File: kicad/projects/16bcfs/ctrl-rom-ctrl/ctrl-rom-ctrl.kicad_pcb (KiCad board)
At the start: 4 copper layers, 0 parts

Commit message: Video 0099 (#147)
Control ROM Control Module PCB Design & Free-Running the Emulator

* Closes #140
* Closes #89
* Closes #141
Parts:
- added C1: 0u1, Capacitor_SMD:C_1206_3216Metric_Pad1.33x1.80mm_HandSolder, B.Cu at (47.0, 48.1)
- added C11: 0u1, Capacitor_SMD:C_1206_3216Metric_Pad1.33x1.80mm_HandSolder, F.Cu at (73.2, 41.7)
- added C12: 0u1, Capacitor_SMD:C_1206_3216Metric_Pad1.33x1.80mm_HandSolder, B.Cu at (94.0, 41.5)
- added C13: 0u1, Capacitor_SMD:C_1206_3216Metric_Pad1.33x1.80mm_HandSolder, F.Cu at (91.2, 41.6)
- added C14: 0u1, Capacitor_SMD:C_1206_3216Metric_Pad1.33x1.80mm_HandSolder, B.Cu at (111.9, 41.6)
- added C15: 0u1, Capacitor_SMD:C_1206_3216Metric_Pad1.33x1.80mm_HandSolder, F.Cu at (73.2, 32.8)
- added C16: 0u1, Capacitor_SMD:C_1206_3216Metric_Pad1.33x1.80mm_HandSolder, B.Cu at (94.0, 32.8)
- added C17: 0u1, Capacitor_SMD:C_1206_3216Metric_Pad1.33x1.80mm_HandSolder, F.Cu at (91.2, 32.8)
- added C18: 0u1, Capacitor_SMD:C_1206_3216Metric_Pad1.33x1.80mm_HandSolder, B.Cu at (111.9, 32.8)
- added C19: 0u1, Capacitor_SMD:C_1206_3216Metric_Pad1.33x1.80mm_HandSolder, B.Cu at (56.4, 48.1)
- added C2: 0u1, Capacitor_SMD:C_1206_3216Metric_Pad1.33x1.80mm_HandSolder, F.Cu at (55.7, 33.3)
- added C20: 0u1, Capacitor_SMD:C_1206_3216Metric_Pad1.33x1.80mm_HandSolder, B.Cu at (34.3, 35.9)
- added C21: 0u1, Capacitor_SMD:C_1206_3216Metric_Pad1.33x1.80mm_HandSolder, F.Cu at (32.1, 62.6)
- added C22: 0u1, Capacitor_SMD:C_1206_3216Metric_Pad1.33x1.80mm_HandSolder, F.Cu at (46.1, 62.6)
- added C23: 0u1, Capacitor_SMD:C_1206_3216Metric_Pad1.33x1.80mm_HandSolder, F.Cu at (43.5, 48.5)
- added C24: 47u, Capacitor_SMD:C_1206_3216Metric_Pad1.33x1.80mm_HandSolder, F.Cu at (108.6, 58.4)
- added C25: 47u, Capacitor_SMD:C_1206_3216Metric_Pad1.33x1.80mm_HandSolder, B.Cu at (31.1, 58.4)
- added C3: 0u1, Capacitor_SMD:C_1206_3216Metric_Pad1.33x1.80mm_HandSolder, B.Cu at (37.4, 48.0)
- added C4: 0u1, Capacitor_SMD:C_1206_3216Metric_Pad1.33x1.80mm_HandSolder, F.Cu at (28.9, 48.6)
- added C5: 0u1, Capacitor_SMD:C_1206_3216Metric_Pad1.33x1.80mm_HandSolder, B.Cu at (74.4, 59.5)
- added C6: 0u1, Capacitor_SMD:C_1206_3216Metric_Pad1.33x1.80mm_HandSolder, F.Cu at (56.2, 48.9)
- added C7: 0u1, Capacitor_SMD:C_1206_3216Metric_Pad1.33x1.80mm_HandSolder, F.Cu at (64.3, 33.4)
- added C8: 0u1, Capacitor_SMD:C_1206_3216Metric_Pad1.33x1.80mm_HandSolder, B.Cu at (93.5, 59.6)
- added C9: 0u1, Capacitor_SMD:C_1206_3216Metric_Pad1.33x1.80mm_HandSolder, B.Cu at (58.4, 32.1)
- added D1: Red, LED_SMD:LED_1206_3216Metric_Pad1.42x1.75mm_HandSolder, F.Cu at (73.0, 65.7)
- added D10: Red, LED_SMD:LED_1206_3216Metric_Pad1.42x1.75mm_HandSolder, F.Cu at (95.9, 65.7)
- added D11: Red, LED_SMD:LED_1206_3216Metric_Pad1.42x1.75mm_HandSolder, F.Cu at (98.4, 65.7)
- added D12: Red, LED_SMD:LED_1206_3216Metric_Pad1.42x1.75mm_HandSolder, F.Cu at (101.0, 65.7)
- added D13: Red, LED_SMD:LED_1206_3216Metric_Pad1.42x1.75mm_HandSolder, F.Cu at (103.5, 65.7)
- added D14: Red, LED_SMD:LED_1206_3216Metric_Pad1.42x1.75mm_HandSolder, F.Cu at (106.0, 65.7)
- added D15: Red, LED_SMD:LED_1206_3216Metric_Pad1.42x1.75mm_HandSolder, F.Cu at (108.6, 65.7)
- added D2: Red, LED_SMD:LED_1206_3216Metric_Pad1.42x1.75mm_HandSolder, F.Cu at (75.6, 65.7)
- added D24: Red, LED_SMD:LED_1206_3216Metric_Pad1.42x1.75mm_HandSolder, F.Cu at (111.1, 65.7)
- added D3: Red, LED_SMD:LED_1206_3216Metric_Pad1.42x1.75mm_HandSolder, F.Cu at (78.1, 65.7)
- added D4: Red, LED_SMD:LED_1206_3216Metric_Pad1.42x1.75mm_HandSolder, F.Cu at (80.6, 65.7)
- added D5: Red, LED_SMD:LED_1206_3216Metric_Pad1.42x1.75mm_HandSolder, F.Cu at (83.2, 65.7)
- added D6: Red, LED_SMD:LED_1206_3216Metric_Pad1.42x1.75mm_HandSolder, F.Cu at (85.7, 65.7)
- added D7: Red, LED_SMD:LED_1206_3216Metric_Pad1.42x1.75mm_HandSolder, F.Cu at (88.3, 65.7)
- added D8: Red, LED_SMD:LED_1206_3216Metric_Pad1.42x1.75mm_HandSolder, F.Cu at (90.8, 65.7)
- added D9: Red, LED_SMD:LED_1206_3216Metric_Pad1.42x1.75mm_HandSolder, F.Cu at (93.3, 65.7)
- added J1: Instruction, Connector_PinHeader_2.54mm:PinHeader_1x16_P2.54mm_Vertical, B.Cu at (69.8, 27.9)
- added J2: Control ROM Address, Connector_PinHeader_2.54mm:PinHeader_1x16_P2.54mm_Vertical, B.Cu at (73.7, 48.3)
- added J3: Raw Address for Pgm ROM, Connector_PinHeader_2.54mm:PinHeader_1x16_P2.54mm_Vertical, B.Cu at (73.7, 27.9)
- added J4: Signal Header, Connector_PinHeader_2.54mm:PinHeader_1x16_P2.54mm_Vertical, B.Cu at (27.9, 27.9)
- added J5: Power, Connector_PinHeader_2.54mm:PinHeader_1x02_P2.54mm_Vertical, B.Cu at (27.9, 57.1)
- added J6: Power, Connector_PinHeader_2.54mm:PinHeader_1x02_P2.54mm_Vertical, B.Cu at (111.8, 57.1)
- added R1: 1K, Resistor_SMD:R_1206_3216Metric_Pad1.30x1.75mm_HandSolder, B.Cu at (73.0, 65.8)
- added R10: 1K, Resistor_SMD:R_1206_3216Metric_Pad1.30x1.75mm_HandSolder, B.Cu at (95.9, 65.8)
- added R11: 1K, Resistor_SMD:R_1206_3216Metric_Pad1.30x1.75mm_HandSolder, B.Cu at (98.4, 65.8)
- added R12: 1K, Resistor_SMD:R_1206_3216Metric_Pad1.30x1.75mm_HandSolder, B.Cu at (101.0, 65.8)
- added R13: 1K, Resistor_SMD:R_1206_3216Metric_Pad1.30x1.75mm_HandSolder, B.Cu at (103.5, 65.8)
- added R14: 1K, Resistor_SMD:R_1206_3216Metric_Pad1.30x1.75mm_HandSolder, B.Cu at (106.0, 65.8)
- added R15: 1K, Resistor_SMD:R_1206_3216Metric_Pad1.30x1.75mm_HandSolder, B.Cu at (108.6, 65.8)
- added R16: 0R, Resistor_SMD:R_1206_3216Metric_Pad1.30x1.75mm_HandSolder, F.Cu at (42.6, 56.9)
- added R17: 0R, Resistor_SMD:R_1206_3216Metric_Pad1.30x1.75mm_HandSolder, F.Cu at (45.1, 56.9)
- added R18: 0R, Resistor_SMD:R_1206_3216Metric_Pad1.30x1.75mm_HandSolder, B.Cu at (64.7, 48.6)
- added R19: 0R, Resistor_SMD:R_1206_3216Metric_Pad1.30x1.75mm_HandSolder, B.Cu at (64.7, 45.9)
- added R2: 1K, Resistor_SMD:R_1206_3216Metric_Pad1.30x1.75mm_HandSolder, B.Cu at (75.6, 65.8)
- added R20: 0R, Resistor_SMD:R_1206_3216Metric_Pad1.30x1.75mm_HandSolder, F.Cu at (47.6, 56.9)
- added R21: 0R, Resistor_SMD:R_1206_3216Metric_Pad1.30x1.75mm_HandSolder, B.Cu at (64.7, 51.3)
- added R22: 0R, Resistor_SMD:R_1206_3216Metric_Pad1.30x1.75mm_HandSolder, F.Cu at (65.2, 63.9)
- added R23: 0R, Resistor_SMD:R_1206_3216Metric_Pad1.30x1.75mm_HandSolder, F.Cu at (65.2, 61.4)
- added R24: 1K, Resistor_SMD:R_1206_3216Metric_Pad1.30x1.75mm_HandSolder, B.Cu at (111.1, 65.8)
- added R25: 0R, Resistor_SMD:R_1206_3216Metric_Pad1.30x1.75mm_HandSolder, B.Cu at (48.5, 38.1)
- added R26: 0R, Resistor_SMD:R_1206_3216Metric_Pad1.30x1.75mm_HandSolder, B.Cu at (43.2, 33.3)
- added R27: 0R, Resistor_SMD:R_1206_3216Metric_Pad1.30x1.75mm_HandSolder, F.Cu at (65.2, 66.4)
- added R28: 0R, Resistor_SMD:R_1206_3216Metric_Pad1.30x1.75mm_HandSolder, F.Cu at (59.9, 63.9)
- added R29: 0R, Resistor_SMD:R_1206_3216Metric_Pad1.30x1.75mm_HandSolder, F.Cu at (59.9, 61.4)
- added R3: 1K, Resistor_SMD:R_1206_3216Metric_Pad1.30x1.75mm_HandSolder, B.Cu at (78.1, 65.8)
- added R30: 0R, Resistor_SMD:R_1206_3216Metric_Pad1.30x1.75mm_HandSolder, F.Cu at (59.9, 66.4)
- added R31: 0R, Resistor_SMD:R_1206_3216Metric_Pad1.30x1.75mm_HandSolder, F.Cu at (33.7, 56.9)
- added R32: 0R, Resistor_SMD:R_1206_3216Metric_Pad1.30x1.75mm_HandSolder, F.Cu at (39.1, 56.9)
- added R33: 0R, Resistor_SMD:R_1206_3216Metric_Pad1.30x1.75mm_HandSolder, F.Cu at (36.4, 56.9)
- added R34: 0R, Resistor_SMD:R_1206_3216Metric_Pad1.30x1.75mm_HandSolder, B.Cu at (38.4, 63.5)
- added R35: 0R, Resistor_SMD:R_1206_3216Metric_Pad1.30x1.75mm_HandSolder, B.Cu at (41.1, 63.5)
- added R36: 0R, Resistor_SMD:R_1206_3216Metric_Pad1.30x1.75mm_HandSolder, B.Cu at (35.7, 63.5)
- added R4: 1K, Resistor_SMD:R_1206_3216Metric_Pad1.30x1.75mm_HandSolder, B.Cu at (80.6, 65.8)
- added R5: 1K, Resistor_SMD:R_1206_3216Metric_Pad1.30x1.75mm_HandSolder, B.Cu at (83.2, 65.8)
- added R6: 1K, Resistor_SMD:R_1206_3216Metric_Pad1.30x1.75mm_HandSolder, B.Cu at (85.7, 65.8)
- added R7: 1K, Resistor_SMD:R_1206_3216Metric_Pad1.30x1.75mm_HandSolder, B.Cu at (88.3, 65.8)
- added R8: 1K, Resistor_SMD:R_1206_3216Metric_Pad1.30x1.75mm_HandSolder, B.Cu at (90.8, 65.8)
- added R9: 1K, Resistor_SMD:R_1206_3216Metric_Pad1.30x1.75mm_HandSolder, B.Cu at (93.3, 65.8)
- added U1: 74HC08, Package_SO:SOIC-14_3.9x8.7mm_P1.27mm, B.Cu at (47.8, 54.4)
- added U11: 74HC157, Package_SO:SOIC-16_3.9x9.9mm_P1.27mm, F.Cu at (79.8, 42.5)
- added U12: 74HC157, Package_SO:SOIC-16_3.9x9.9mm_P1.27mm, B.Cu at (87.4, 42.5)
- added U13: 74HC157, Package_SO:SOIC-16_3.9x9.9mm_P1.27mm, F.Cu at (97.8, 42.5)
- added U14: 74HC157, Package_SO:SOIC-16_3.9x9.9mm_P1.27mm, B.Cu at (105.4, 42.5)
- added U15: 74HC193, Package_SO:SOIC-16_3.9x9.9mm_P1.27mm, F.Cu at (79.8, 33.7)
- added U16: 74HC193, Package_SO:SOIC-16_3.9x9.9mm_P1.27mm, B.Cu at (87.4, 33.7)
- added U17: 74HC193, Package_SO:SOIC-16_3.9x9.9mm_P1.27mm, F.Cu at (97.8, 33.7)
- added U18: 74HC193, Package_SO:SOIC-16_3.9x9.9mm_P1.27mm, B.Cu at (105.4, 33.7)
- added U19: 74HC04, Package_SO:SOIC-14_3.9x8.7mm_P1.27mm, B.Cu at (57.2, 54.4)
- added U2: 74HC74, Package_SO:SOIC-14_3.9x8.7mm_P1.27mm, F.Cu at (54.9, 39.3)
- added U21: 74HC08, Package_SO:SOIC-14_3.9x8.7mm_P1.27mm, F.Cu at (38.1, 63.5)
- added U22: 74HC08, Package_SO:SOIC-14_3.9x8.7mm_P1.27mm, F.Cu at (52.1, 63.5)
- added U23: 74HC32, Package_SO:SOIC-14_3.9x8.7mm_P1.27mm, F.Cu at (49.5, 49.5)
- added U3: 74HC03, Package_SO:SOIC-14_3.9x8.7mm_P1.27mm, B.Cu at (38.3, 54.4)
- added U4: 74HC193, Package_SO:SOIC-16_3.9x9.9mm_P1.27mm, F.Cu at (35.6, 49.5)
- added U5: 74HC541, Package_SO:SOIC-20W_7.5x12.8mm_P1.27mm, B.Cu at (82.5, 56.5)
- added U6: 74HC00, Package_SO:SOIC-14_3.9x8.7mm_P1.27mm, F.Cu at (62.2, 49.7)
- added U7: 74HC00, Package_SO:SOIC-14_3.9x8.7mm_P1.27mm, F.Cu at (63.4, 39.4)
- added U8: 74HC541, Package_SO:SOIC-20W_7.5x12.8mm_P1.27mm, B.Cu at (101.6, 56.5)
- added U9: 74HC165, Package_SO:SOIC-16_3.9x9.9mm_P1.27mm, B.Cu at (59.3, 38.7)
- added X1: XO32, eryjus:Oscillator_DIP-8-14, F.Cu at (31.8, 41.9)
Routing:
- net GNDREF: track 0.00 -> 613.1 mm, vias 0 -> 105
- net VCC: track 0.00 -> 303.4 mm, vias 0 -> 39
- net ~{QR}: track 0.00 -> 184.6 mm, vias 0 -> 2
- net ~{DONE}: track 0.00 -> 123.5 mm, vias 0 -> 8
- net CPY_CLK: track 0.00 -> 110.1 mm, vias 0 -> 1
- net SRAM ~{CE}: track 0.00 -> 100.7 mm, vias 0 -> 2
- net ~{Raw_Cpy_Clk}: track 0.00 -> 89.5 mm, vias 0 -> 4
- net ~{RESET}: track 0.00 -> 72.2 mm, vias 0 -> 2
- net QS: track 0.00 -> 71.9 mm, vias 0 -> 4
- net Addr Counter ~{CO}: track 0.00 -> 71.4 mm, vias 0 -> 3
- net QC: track 0.00 -> 64.5 mm, vias 0 -> 8
- net RAW_CPY_CLK: track 0.00 -> 61.7 mm, vias 0 -> 2
- net Net-(U19-Pad13): track 0.00 -> 60.3 mm, vias 0 -> 3
- net INSTR_AC: track 0.00 -> 56.1 mm, vias 0 -> 3
- net INSTR_AE: track 0.00 -> 54.2 mm, vias 0 -> 1
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- added copper zone on B.Cu, net GNDREF
- added copper zone on F.Cu, net GNDREF
- added copper zone on In1.Cu, net GNDREF
- added copper zone on In2.Cu, net VCC
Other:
- board outline added: 88.9 x 43.2 mm
- board text added: "0R"
- board text added: "0u1"
- board text added: "16-Bit Computer From Scratch"
- board text added: "47u"
- board text added: "74HC00"
- board text added: "74HC03"
- board text added: "74HC04"
- board text added: "74HC08"
- board text added: "74HC157"
- board text added: "74HC165"
- board text added: "74HC193"
- board text added: "74HC32"
- board text added: "74HC541"
- board text added: "74HC74"
- board text added: "A"
- board text added: "AND3C"
- board text added: "AND3D"
- board text added: "B"
- board text added: "Control ROM Control Module"
- board text added: "Ctrl ROM Address"
- board text added: "ERYJUS"
- board text added: "GND"
- board text added: "Instruction"
- board text added: "Local Xtal"
- board text added: "NAND2C"
- board text added: "Raw Addr for Pgm ROM"
- board text added: "Raw Sys Clk"
- board text added: "Signals"
- board text added: "VCC"
- board text added: "VCC GND"
- board text added: "Y"
- board text added: "oNANDB"
- board text added: "oNANDC"
- board text added: "oNANDD"
- board text added: "v1.0"

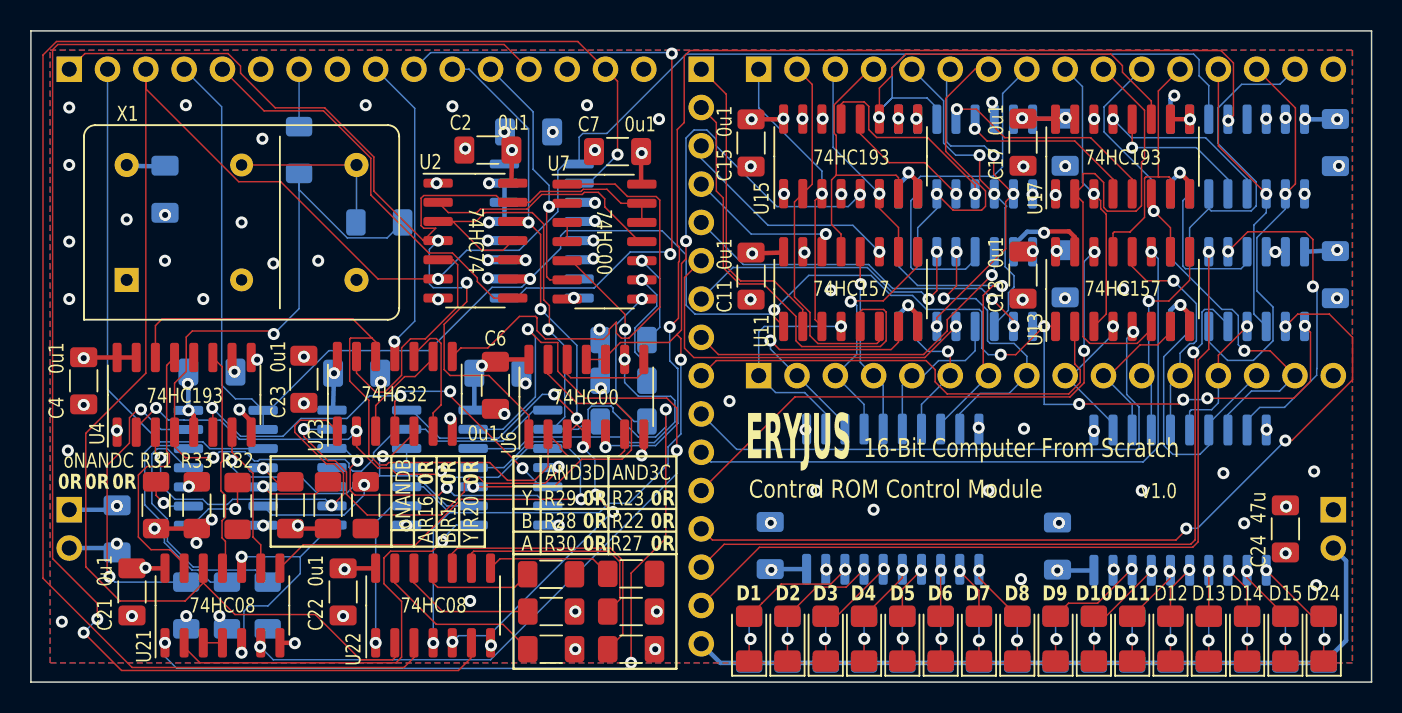
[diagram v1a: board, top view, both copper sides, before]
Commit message: Complete the existing bodge on the PCB
An existing bodge was updated in the schematic and this was extended to
the PCB design of the Control ROM Control Module.

Additionally, the footprints were updated.

I also took the opportunity to update a trace which bounced around a
bit.
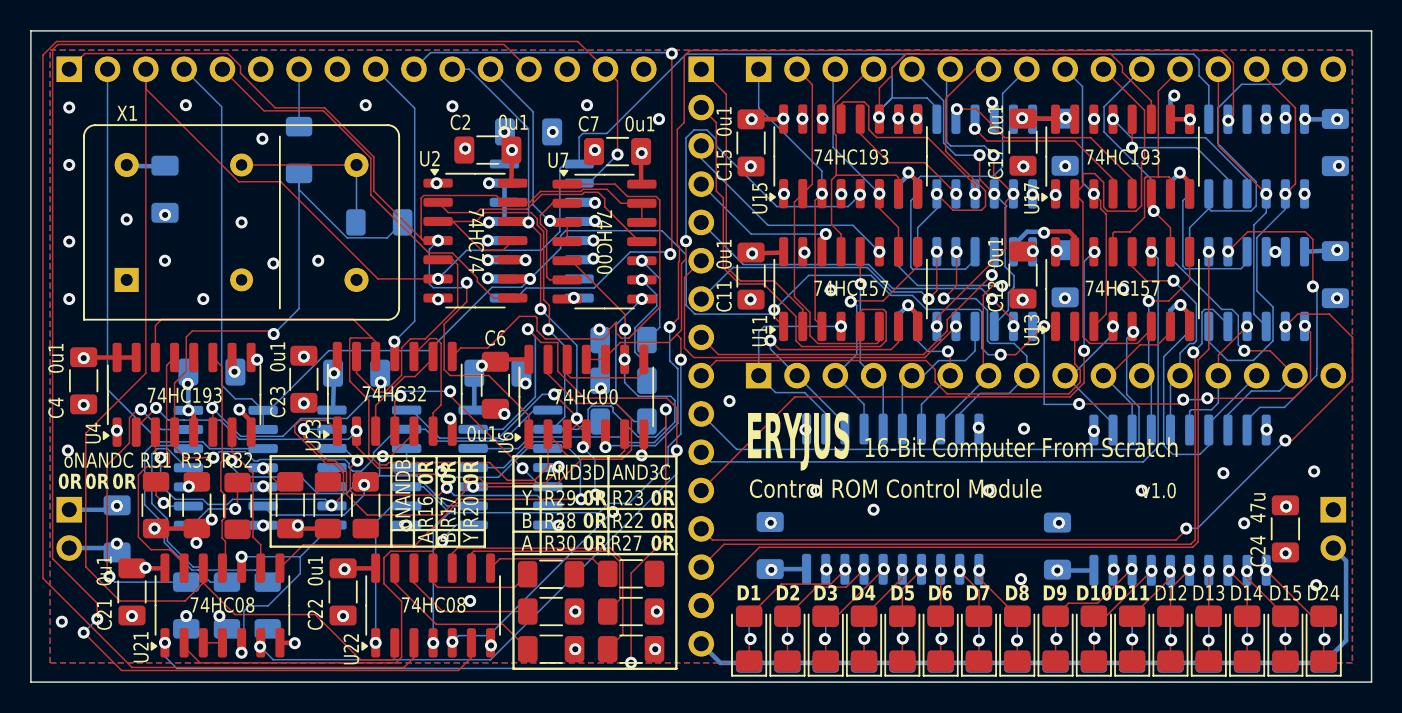
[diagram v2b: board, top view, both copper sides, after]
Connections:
- J4 pad 12: ~{QL} -> QL
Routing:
- net QL: track 1.27 -> 15.4 mm, vias 0 -> 1
- net ~{QL}: track 18.2 -> 7.80 mm, vias 1 -> 0
- net ~{RESET}: track 72.2 -> 71.1 mm
- net ~{QR}: track 184.6 -> 185.4 mm

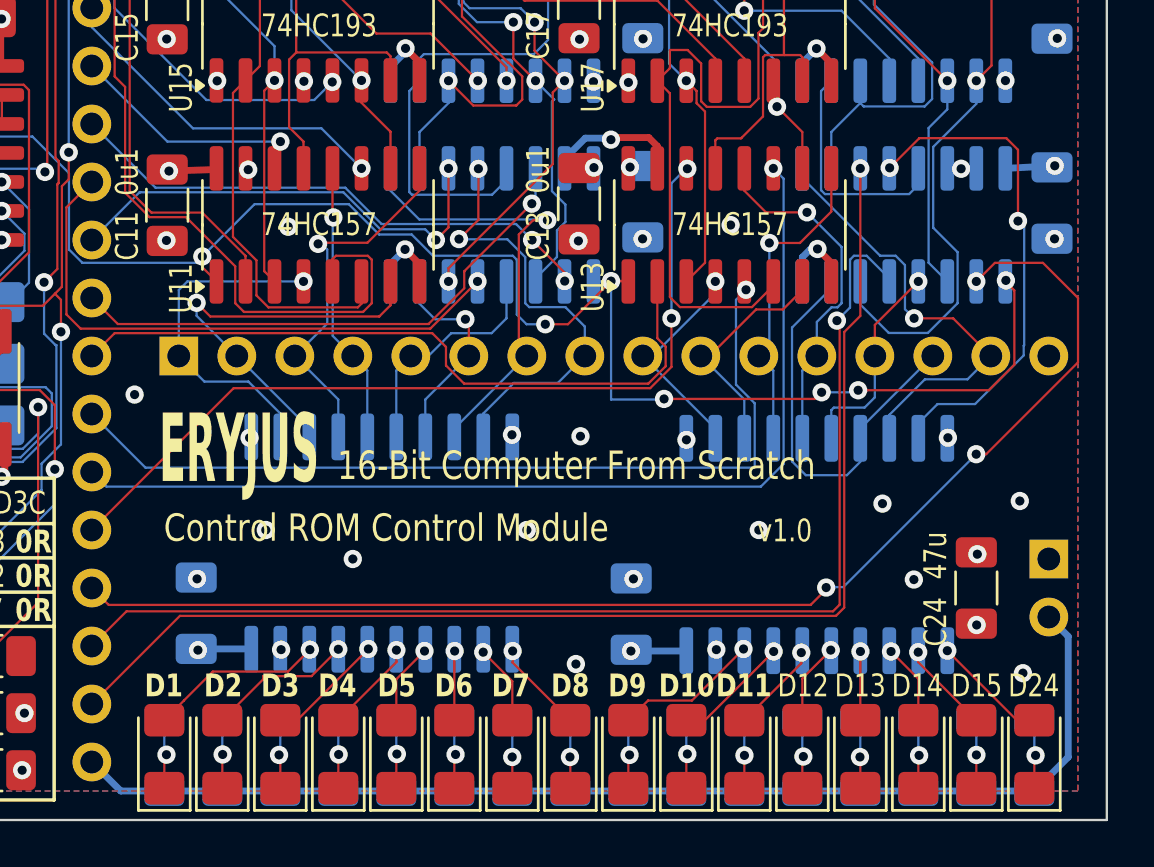
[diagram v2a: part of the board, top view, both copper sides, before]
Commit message: Remove the LEDs from the Control ROM Control Module
The LEDs are not populated on the first iteration PCB.  Remove them from
the schematic and from the PCB design.
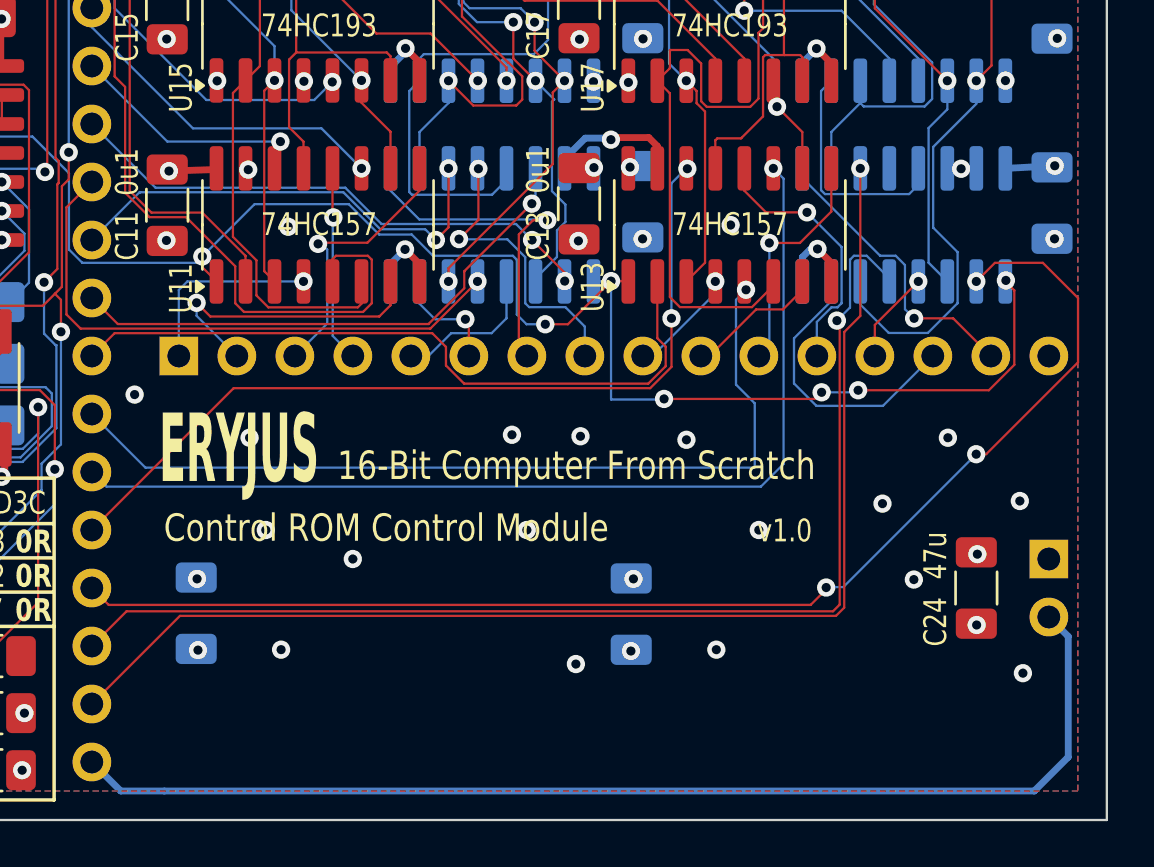
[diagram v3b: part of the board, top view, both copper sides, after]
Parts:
- removed D1, D10, D11, D12, D13, D14, D15, D2, D24, D3, D4, D5, D6, D7, D8, D9: Red, LED_SMD:LED_1206_3216Metric_Pad1.42x1.75mm_HandSolder
- removed R1, R10, R11, R12, R13, R14, R15, R2, R24, R3, R4, R5, R6, R7, R8, R9: 1K, Resistor_SMD:R_1206_3216Metric_Pad1.30x1.75mm_HandSolder
- removed U5, U8: 74HC541, Package_SO:SOIC-20W_7.5x12.8mm_P1.27mm
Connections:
- U14 pad 12: ROM_AF -> unconnected-(U14-Zd-Pad12)
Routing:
- net ROM_AF: track 21.3 -> 0.00 mm, vias 2 -> 0
- net Net-(D1-A): track 7.66 -> 0.00 mm, vias 1 -> 0
- net ROM_AE: track 19.2 -> 12.6 mm
- net ROM_A0: track 15.0 -> 8.51 mm
- net ROM_A7: track 19.5 -> 13.0 mm
- net Net-(D2-A): track 6.45 -> 0.00 mm, vias 1 -> 0
- net Net-(D9-A): track 6.34 -> 0.00 mm, vias 1 -> 0
- net ROM_AC: track 9.24 -> 4.05 mm
- net VCC: track 303.4 -> 298.6 mm
- net ROM_AD: track 17.3 -> 12.5 mm
- net ROM_A6: track 19.4 -> 14.9 mm
- net ROM_A8: track 8.89 -> 4.40 mm
- net ROM_A1: track 17.5 -> 13.0 mm
- net Net-(D3-A): track 4.41 -> 0.00 mm, vias 1 -> 0
- net ROM_A9: track 9.65 -> 5.26 mm
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
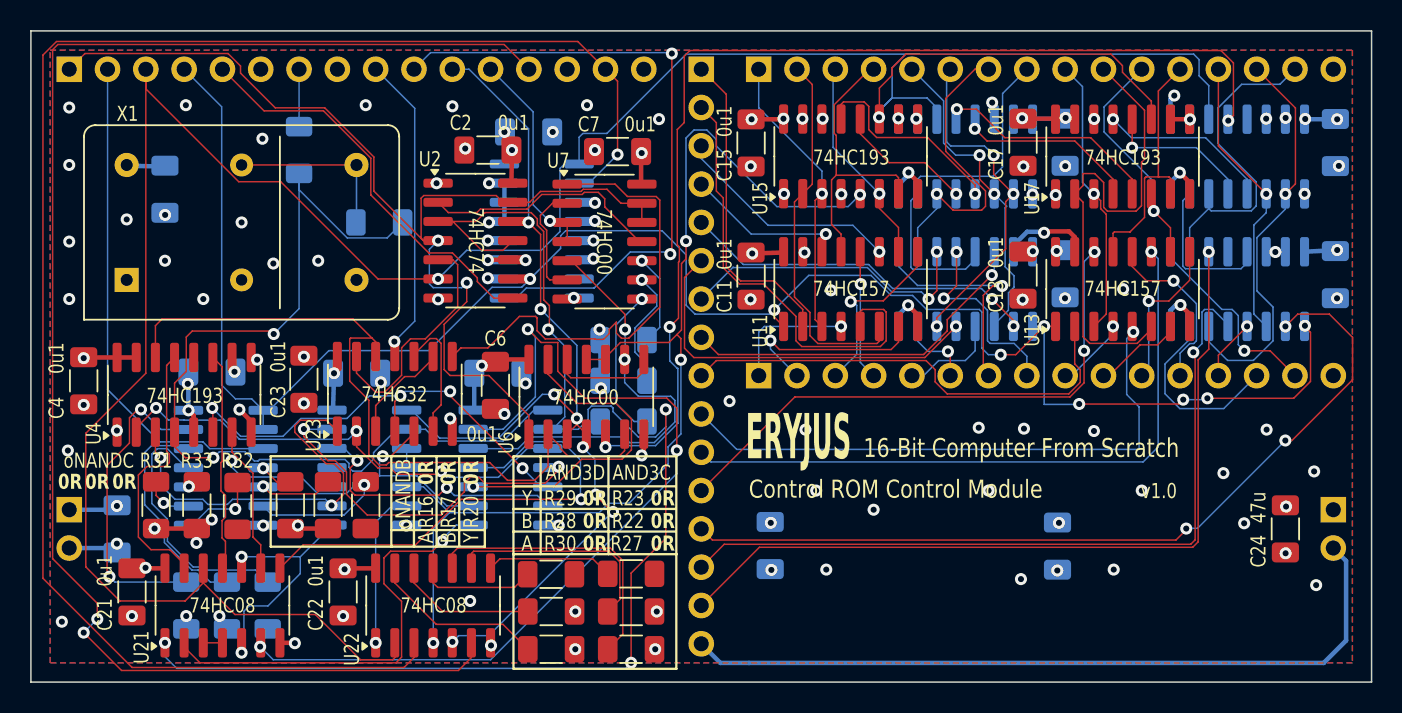
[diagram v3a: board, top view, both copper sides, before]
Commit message: Resolve the Control ROM Control pin alignment
This resulted in a major change to the PCB layout.
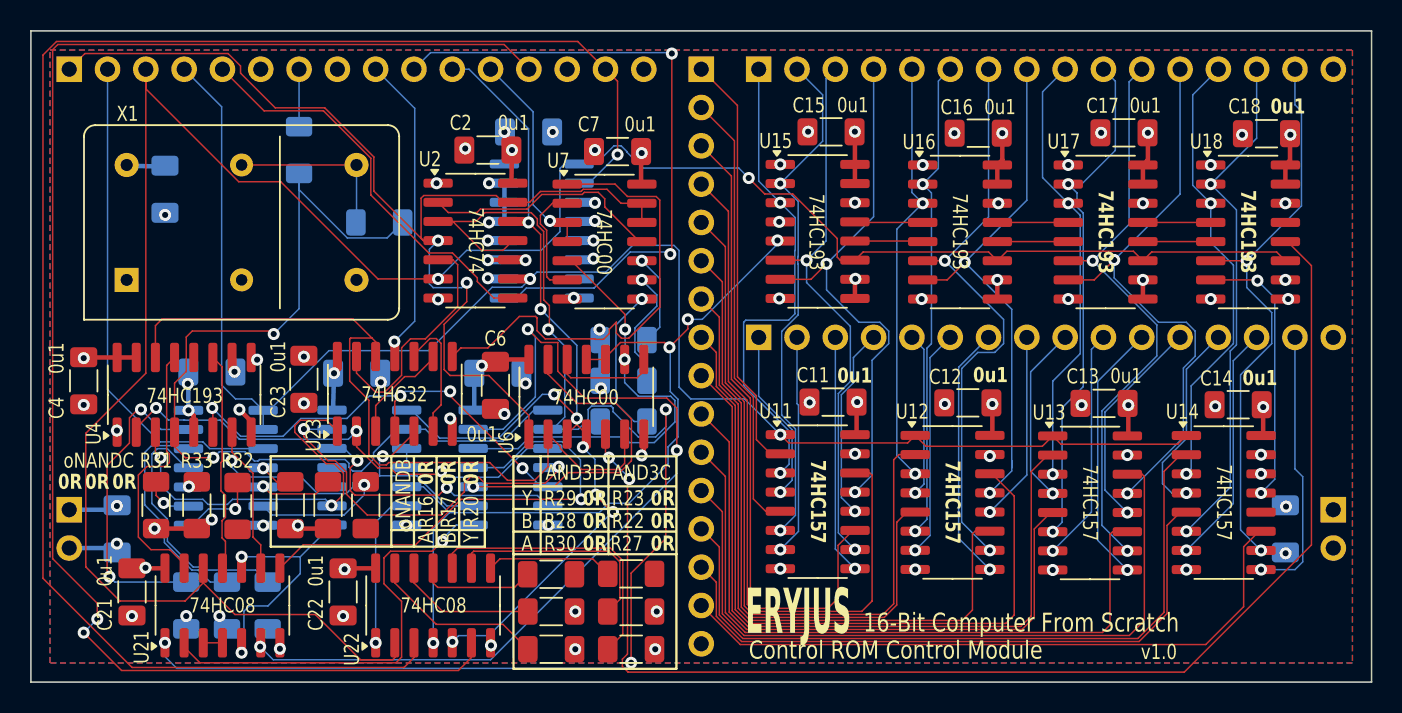
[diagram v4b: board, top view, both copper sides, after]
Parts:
- removed C5, C8: 0u1, Capacitor_SMD:C_1206_3216Metric_Pad1.33x1.80mm_HandSolder
- C12, C14, C16, C18, U12, U14, U16, U18: moved to F.Cu
- C24: moved to B.Cu
- moved U13 14.3 mm to (95.6, 56.7), turned to 0 degrees
- moved U11 14.3 mm to (77.6, 56.6), turned to 0 degrees
- moved U14 14.2 mm to (104.5, 56.7), turned to 0 degrees
- moved U12 14.2 mm to (86.5, 56.7), turned to 0 degrees
- moved C14 10.8 mm to (105.5, 50.2), turned to 180 degrees
- moved C12 10.7 mm to (87.5, 50.1), turned to 180 degrees
- moved C13 10.1 mm to (96.6, 50.1), turned to 180 degrees
- moved C11 9.97 mm to (78.6, 50.0), turned to 180 degrees
- moved C17 6.72 mm to (97.9, 32.2), turned to 180 degrees
- moved C16 5.80 mm to (88.2, 32.2), turned to 180 degrees
- moved U15 5.44 mm to (77.6, 38.7), turned to 0 degrees
- moved C15 5.35 mm to (78.5, 32.1), turned to 180 degrees
- moved U17 5.13 mm to (96.7, 38.7), turned to 0 degrees
- moved U18 5.05 mm to (106.1, 38.7), turned to 0 degrees
- moved U16 5.02 mm to (87.0, 38.7), turned to 0 degrees
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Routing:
- net INSTR_A3: track 10.00 -> 47.4 mm, vias 1 -> 0
- net GNDREF: track 613.1 -> 577.7 mm, vias 105 -> 70
- net ~{QR}: track 185.4 -> 154.2 mm
- net INSTR_A2: track 15.2 -> 42.8 mm, vias 1 -> 0
- net INSTR_A4: track 23.8 -> 48.2 mm, vias 2 -> 0
- net INSTR_A6: track 19.7 -> 44.0 mm, vias 2 -> 0
- net INSTR_A7: track 24.0 -> 48.1 mm, vias 1 -> 0
- net PGM_AA: track 16.2 -> 38.9 mm, vias 1 -> 2
- net PGM_A2: track 13.7 -> 36.4 mm, vias 1 -> 2
- net PGM_AB: track 16.9 -> 38.7 mm, vias 0 -> 2
- net ~{DONE}: track 123.5 -> 104.0 mm, vias 8 -> 2
- net PGM_A6: track 19.9 -> 38.8 mm, vias 1 -> 2
- net QS: track 71.9 -> 53.4 mm
- net VCC: track 298.6 -> 316.7 mm, vias 39 -> 34
- net PGM_A3: track 18.8 -> 36.3 mm, vias 0 -> 2
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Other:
- board text removed: "74HC541"
- board text removed: "VCC GND"
